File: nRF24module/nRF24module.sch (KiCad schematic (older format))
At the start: 31 parts, among them J1 SMA-RP, U1 nRF24L01P, U2 RFX2401C, X1 16MHz

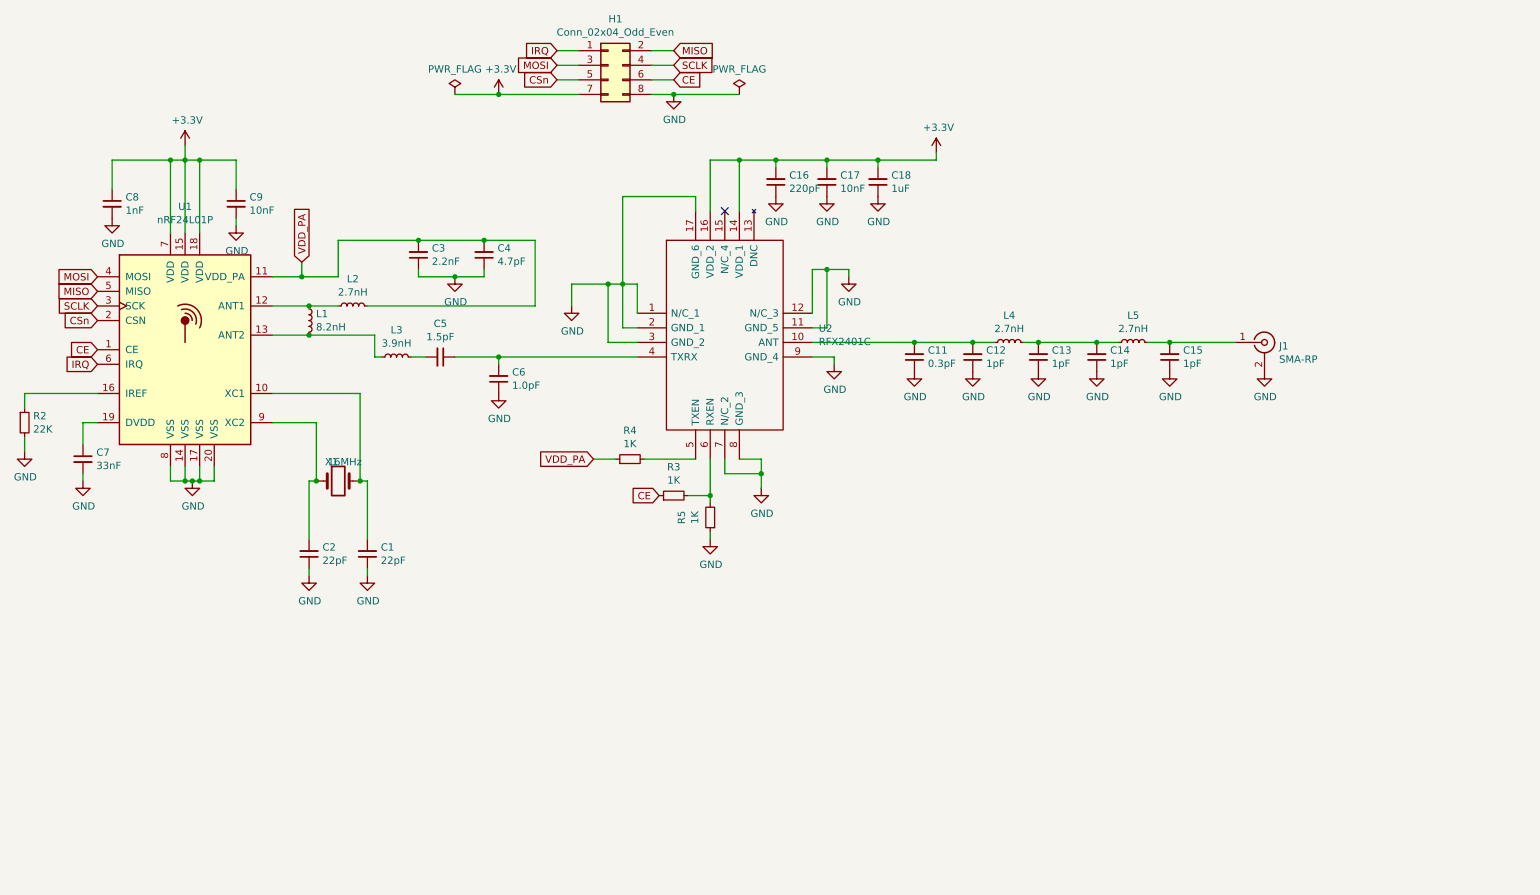
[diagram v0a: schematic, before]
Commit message: Update, with Licence added to files, and rerouted PCB, cleaned up some things. Tightened up components, placed traces neater, placed vias neater. Added OSHW logo. TODO: Make own logo and add that.
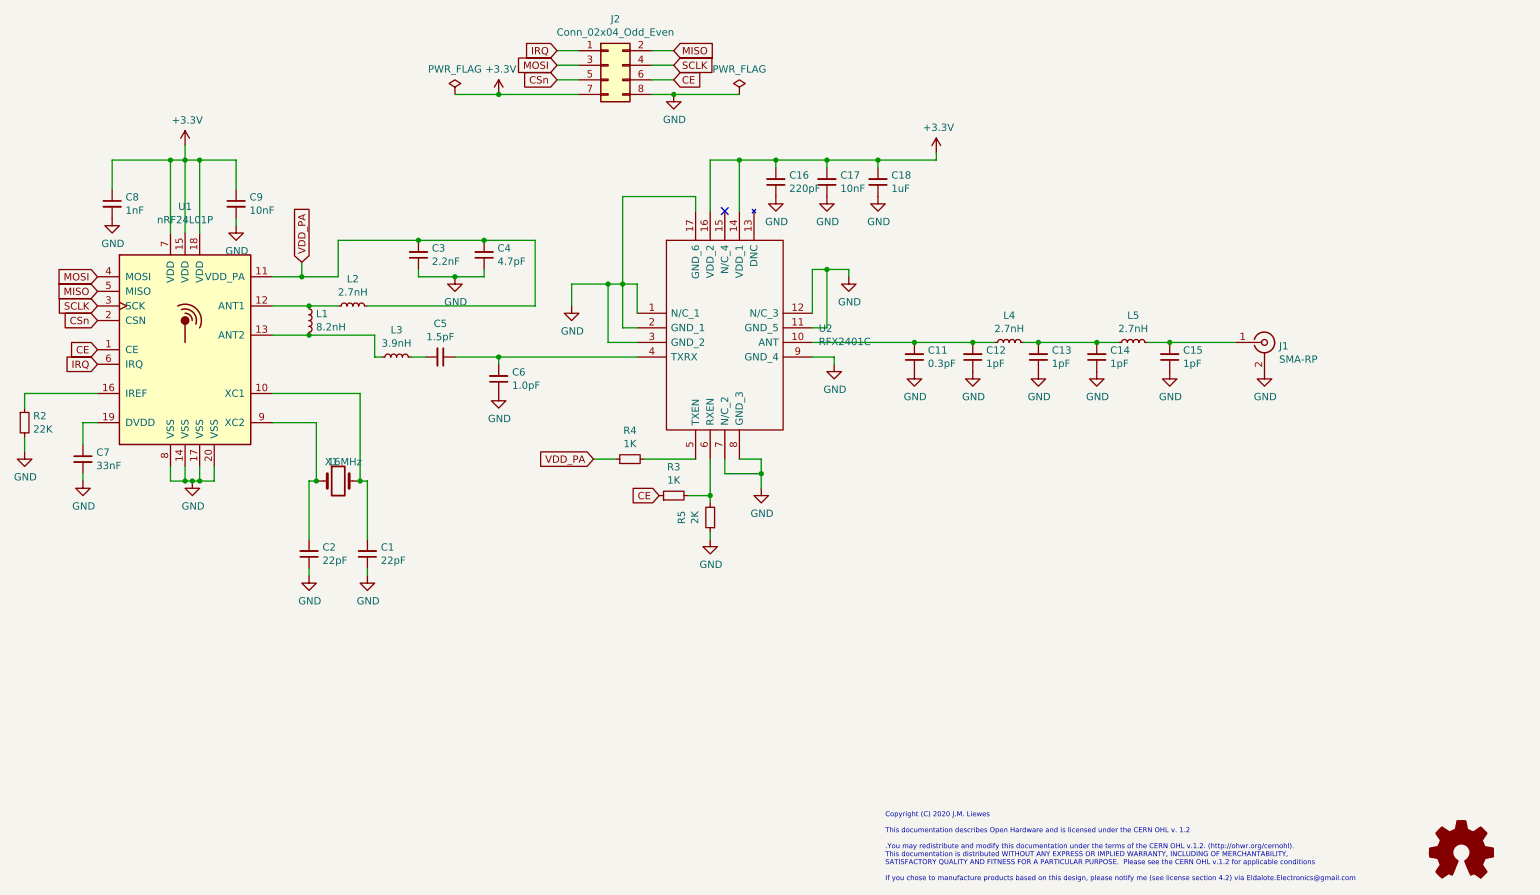
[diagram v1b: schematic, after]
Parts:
- added LOGO1: Logo_Open_Hardware_Small, Symbol:OSHW-Logo2_7.3x6mm_SilkScreen, symbol Graphic:Logo_Open_Hardware_Small
- C1, C2: JLC Part Nr C1555 -> (none); LCSC (none) -> C1555
- C11: JLC Part Nr C170140 -> (none); LCSC (none) -> C170140
- C12, C13, C14, C15, C6: JLC Part Nr C1550 -> (none); LCSC (none) -> C1550
- C16: JLC Part Nr C1530 -> (none); LCSC (none) -> C1530
- C17, C9: JLC Part Nr C15195 -> (none); LCSC (none) -> C15195
- C18: JLC Part Nr C52923 -> (none); LCSC (none) -> C52923
- C3: JLC Part Nr C1531 -> (none); LCSC (none) -> C1531
- C4: JLC Part Nr C1569 -> (none); LCSC (none) -> C1569
- C5: JLC Part Nr C1552 -> (none); LCSC (none) -> C1552
- C7: JLC Part Nr C1585 -> (none); LCSC (none) -> C1585
- C8: JLC Part Nr C1523 -> (none); LCSC (none) -> C1523
- L1: JLC Part Nr C16208 -> (none); LCSC (none) -> C16208
- L2, L4, L5: JLC Part Nr C27123 -> (none); LCSC (none) -> C27123
- L3: JLC Part Nr C14033 -> (none); LCSC (none) -> C14033
- R2: JLC Part Nr C25768 -> (none); LCSC (none) -> C25768
- R3, R4: JLC Part Nr C11702 -> (none); LCSC (none) -> C11702
- R5: value 1K -> 2K; JLC Part Nr C11702 -> (none); LCSC (none) -> C4109
- U1: JLC Part Nr C8791 -> (none); LCSC (none) -> C8791
- U2: JLC Part Nr C19213 -> (none); LCSC (none) -> C19213
- X1: JLC Part Nr C13738 -> (none); LCSC (none) -> C13738
- renumbered H1 to J2
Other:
- note added: "Copyright (C) 2020 J.M. Liewes\n\nThis documentation describes Open Hardware and is licensed under the CERN OHL v. 1.2\n\n.You may redistribute and modify this documentation under the terms of the CERN OHL v.1.2. (http://ohwr.org/cernohl). \nThis documentation is distributed WITHOUT ANY EXPRESS OR IMPLIED WARRANTY, INCLUDING OF MERCHANTABILITY, \nSATISFACTORY QUALITY AND FITNESS FOR A PARTICULAR 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"

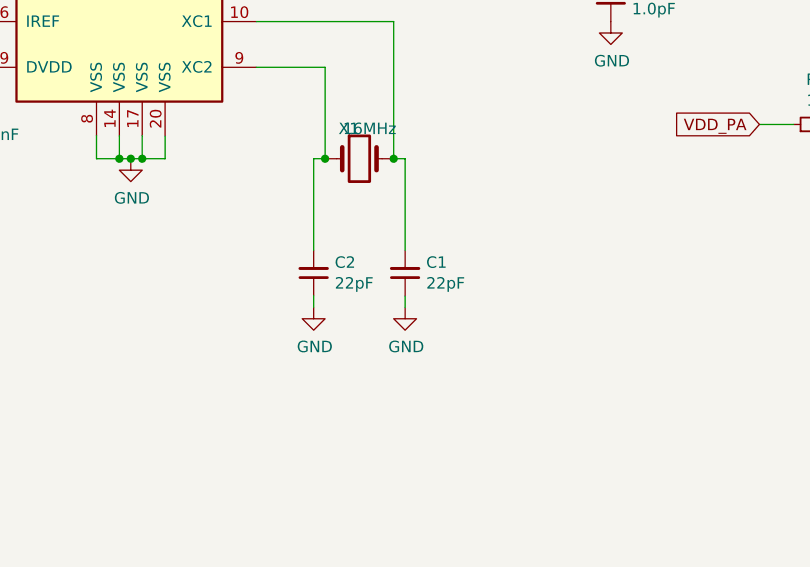
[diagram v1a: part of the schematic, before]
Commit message: Corrected crystal load capacitance.
Signed-off-by: Jan Mart Liewes <Eldalote.Electronics@gmail.com>
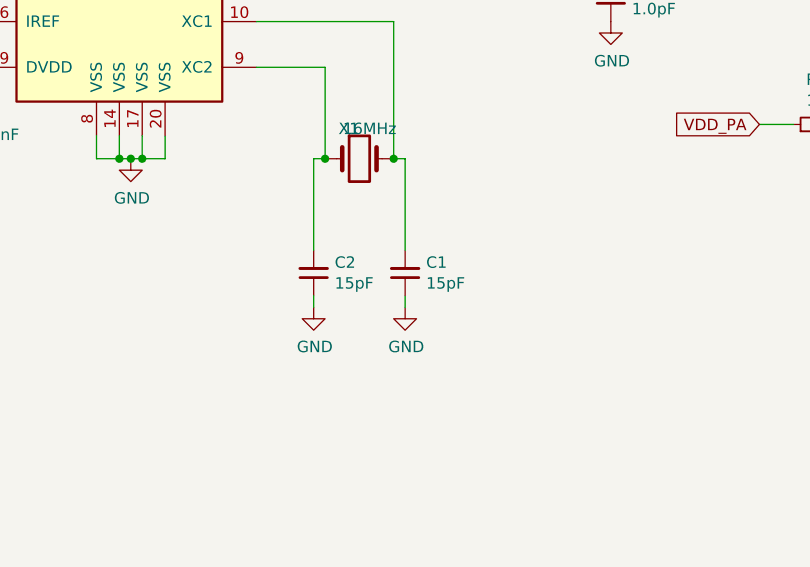
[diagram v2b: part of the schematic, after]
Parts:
- C1, C2: value 22pF -> 15pF; LCSC C1555 -> C1548
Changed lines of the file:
@@
 P 3050 4850
 F 0 "C2" H 2958 4804 50  0000 R CNN
-F 1 "22pF" H 2958 4895 50  0000 R CNN
+F 1 "15pF" H 2958 4895 50  0000 R CNN
 F 2 "Capacitor_SMD:C_0402_1005Metric" H 3088 4700 50  0001 C CNN
 F 3 "~" H 3050 4850 50  0001 C CNN
 F 4 "" V 3050 4850 50  0001 C CNN "JLC Part Nr"
-F 5 " C1555" H 3050 4850 50  0001 C CNN "LCSC"
+F 5 " C1548" H 3050 4850 50  0001 C CNN "LCSC"
 	1    3050 4850
 	-1   0    0    1
@@
 P 3450 4850
 F 0 "C1" H 3358 4804 50  0000 R CNN
-F 1 "22pF" H 3358 4895 50  0000 R CNN
+F 1 "15pF" H 3358 4895 50  0000 R CNN
 F 2 "Capacitor_SMD:C_0402_1005Metric" H 3488 4700 50  0001 C CNN
 F 3 "~" H 3450 4850 50  0001 C CNN
-F 4 " C1555" V 3450 4850 50  0001 C CNN "LCSC"
+F 4 " C1548" V 3450 4850 50  0001 C CNN "LCSC"
 	1    3450 4850
 	-1   0    0    1
